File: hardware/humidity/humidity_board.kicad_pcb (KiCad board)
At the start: 2 copper layers, 99 x 20 mm, 23 parts, among them IC1 ATMEGA88-A, J1 RJ45, P1 ISP, P2 UART, SW1 SW_RESET, U1 ST485, U2 HYT271, m3_loch VAL**

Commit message: fill
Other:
- board size 99 x 20 mm -> 100 x 20 mm
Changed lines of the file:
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@@
     (area 7.399999 74 244.600001 124.2)
     (thickness 1.6)
-    (drawings 13)
+    (drawings 16)
     (tracks 271)
     (zones 0)
@@
     )
   )
+  (dimension 5 (width 0.3) (layer Cmts.User)
+    (gr_text "5.000 mm" (at 202.5 58.650001) (layer Cmts.User)
+      (effects (font (size 1.5 1.5) (thickness 0.3)))
+    )
+    (feature1 (pts (xy 200 88) (xy 200 57.300001)))
+    (feature2 (pts (xy 205 88) (xy 205 57.300001)))
+    (crossbar (pts (xy 205 60.000001) (xy 200 60.000001)))
+    (arrow1a (pts (xy 200 60.000001) (xy 201.126503 59.413581)))
+    (arrow1b (pts (xy 200 60.000001) (xy 201.126503 60.586421)))
+    (arrow2a (pts (xy 205 60.000001) (xy 203.873497 59.413581)))
+    (arrow2b (pts (xy 205 60.000001) (xy 203.873497 60.586421)))
+  )
+  (gr_line (start 200 106) (end 199 106) (angle 90) (layer Edge.Cuts) (width 0.1))
+  (gr_line (start 200 86) (end 200 106) (angle 90) (layer Edge.Cuts) (width 0.1))
+  (gr_line (start 199 86) (end 200 86) (angle 90) (layer Edge.Cuts) (width 0.1))
   (gr_line (start 199 106) (end 133.5 106) (angle 90) (layer Edge.Cuts) (width 0.1))
-  (gr_line (start 199 86) (end 199 106) (angle 90) (layer Edge.Cuts) (width 0.1))
   (gr_line (start 133.5 86) (end 199 86) (angle 90) (layer Edge.Cuts) (width 0.1))
   (dimension 100 (width 0.3) (layer Cmts.User)

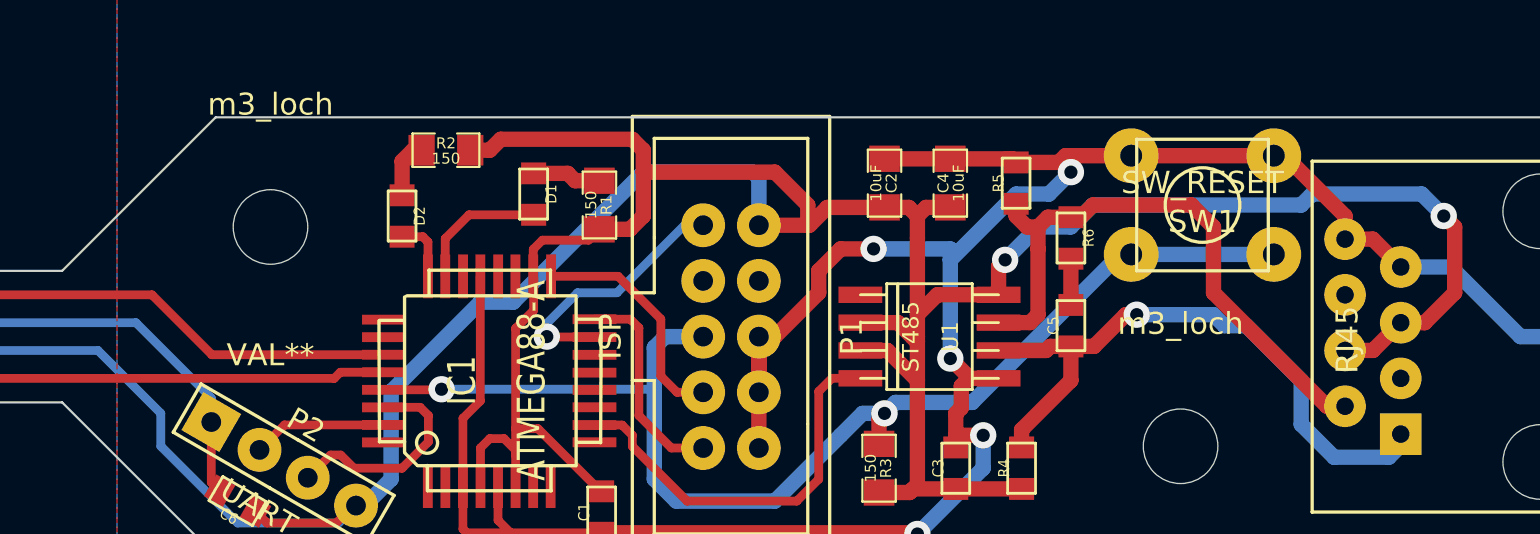
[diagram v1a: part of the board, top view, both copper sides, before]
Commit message: humidity led pos + zones
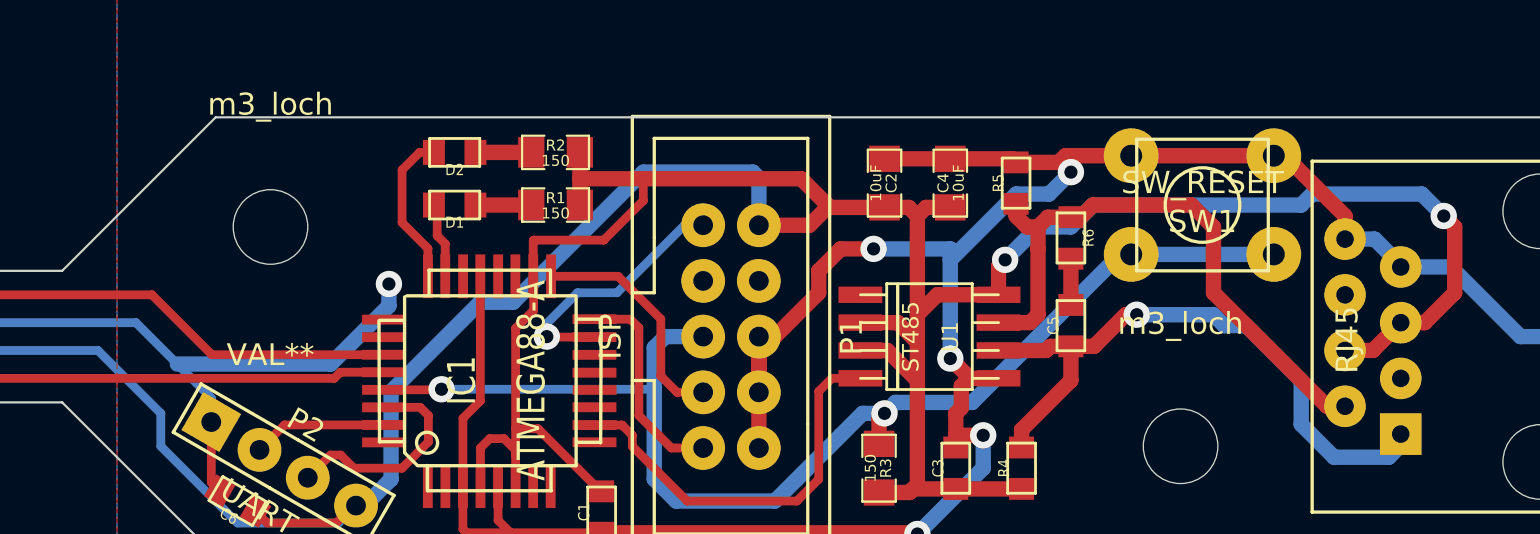
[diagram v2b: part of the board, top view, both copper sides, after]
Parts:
- moved R2 5.00 mm to (149.0, 87.6)
- moved D2 3.76 mm to (144.4, 87.6), turned to 180 degrees
- moved D1 3.63 mm to (144.4, 90.0), turned to 180 degrees
- moved R1 2.00 mm to (149.0, 90.0), turned to 0 degrees
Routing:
- net GND: track 170.8 -> 182.6 mm, vias 5 -> 6
- net VCC: track 196.3 -> 191.8 mm
- net /LED2: track 2.85 -> 7.13 mm
- net /LED1: track 6.20 -> 3.46 mm
- net N-0000016: track 3.14 -> 2.55 mm

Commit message: finalized boards for production
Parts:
- R3: value 150 -> 10k; footprint SM0805_big -> SM0603_big
- moved R3 0.05 mm to (163.7, 102.0)
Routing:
- net GND: track 182.6 -> 184.4 mm, vias 6 -> 5
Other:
- outline, holes or cut-outs redrawn

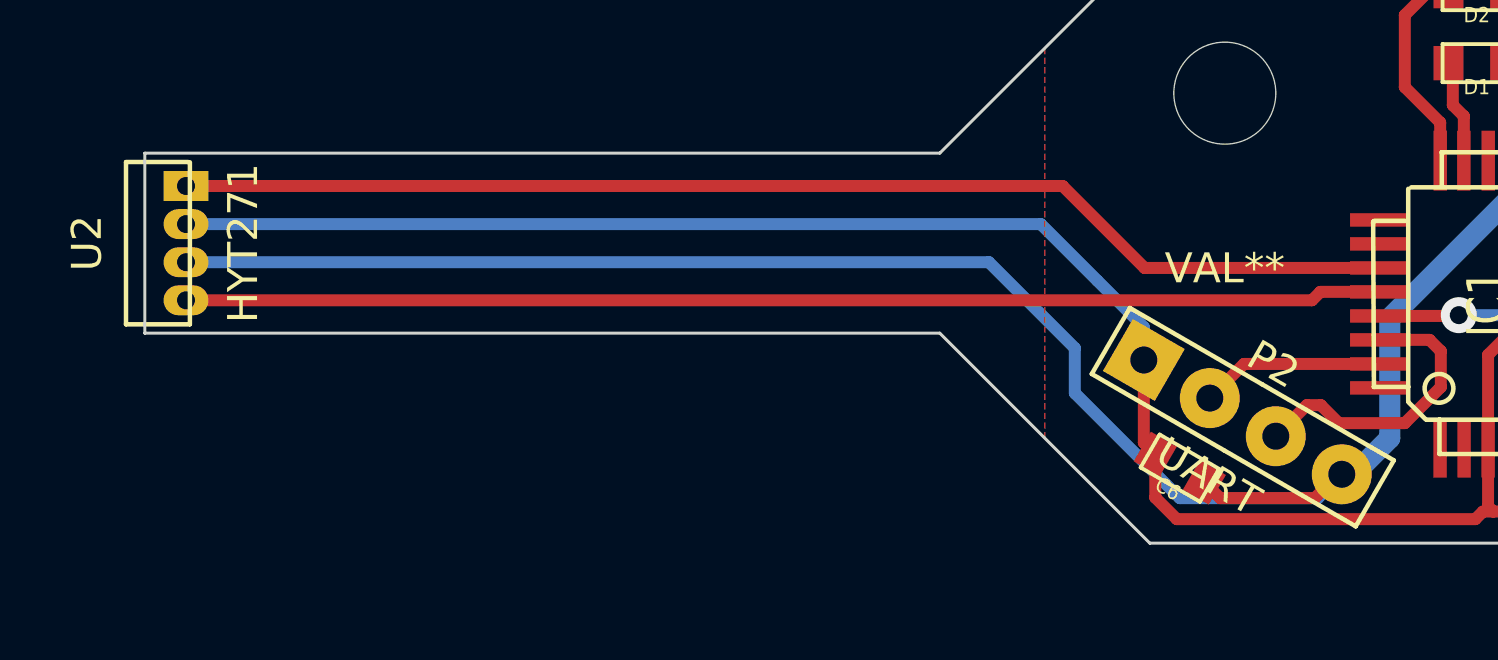
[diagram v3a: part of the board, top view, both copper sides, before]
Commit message: added i2c pullups to humidity board
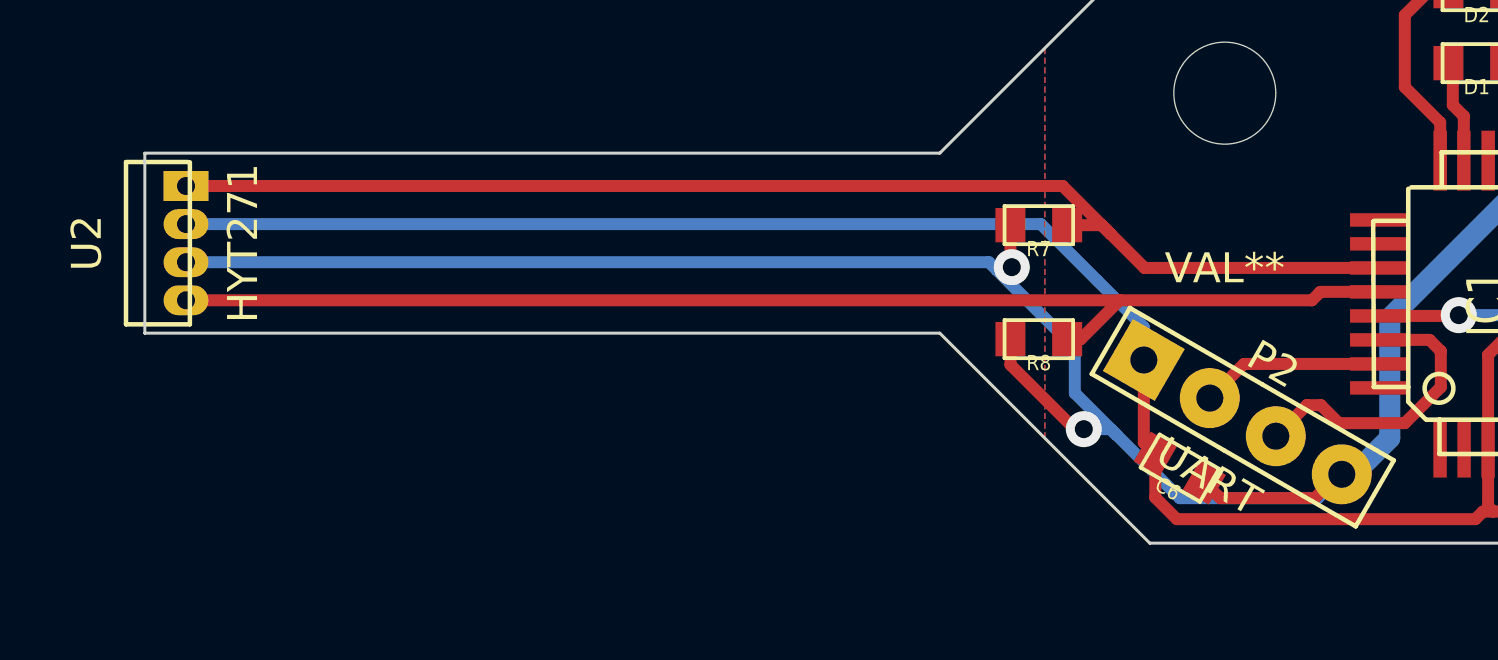
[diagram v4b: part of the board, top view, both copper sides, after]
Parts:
- added R7: 2k2, SM0603_big, F.Cu at (129.8, 95.4)
- added R8: 2k2, SM0603_big, F.Cu at (129.8, 99.2)
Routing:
- net VCC: track 191.8 -> 199.1 mm, vias 2 -> 4
- net /SCL: track 39.9 -> 42.2 mm
- net /SDA: track 40.9 -> 42.5 mm
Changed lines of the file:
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@@
 (kicad_pcb (version 3) (host pcbnew "(2013-may-18)-stable")
   (general
-    (links 62)
+    (links 66)
     (no_connects 0)
     (area 99.949999 85.949999 200.050001 106.050001)
     (thickness 1.6)
     (drawings 8)
-    (tracks 277)
+    (tracks 297)
     (zones 0)
-    (modules 23)
+    (modules 25)
     (nets 19)
   )
@@
   (net 13 /zb)
   (net 14 GND)
-  (net 15 N-0000014)
-  (net 16 N-0000015)
-  (net 17 N-0000016)
+  (net 15 N-0000015)
+  (net 16 N-0000017)
+  (net 17 N-000002)
   (net 18 VCC)
   (net_class Default "This is the default net class."
@@
     (add_net /zb)
     (add_net GND)
-    (add_net N-0000014)
     (add_net N-0000015)
-    (add_net N-0000016)
-    (add_net VCC)
+    (add_net N-0000017)
+    (add_net N-000002)
   )
   (net_class uc ""
@@
     (add_net /SDA)
     (add_net /TX)
+    (add_net VCC)
   )
   (module wannenstecker_2x5_rm254 (layer F.Cu)
@@
     (pad 1 smd rect (at -1.108 0) (size 1.2 1.397)
       (layers F.Cu F.Paste F.Mask)
-      (net 16 N-0000015)
+      (net 16 N-0000017)
     )
     (pad 2 smd rect (at 1.108 0) (size 1.2 1.397)
@@
     (pad 1 smd rect (at -1.108 0) (size 1.2 1.397)
       (layers F.Cu F.Paste F.Mask)
-      (net 17 N-0000016)
+      (net 17 N-000002)
     )
     (pad 2 smd rect (at 1.108 0) (size 1.2 1.397)
@@
     (pad 2 smd rect (at 0.945 0 90) (size 1 1.143)
       (layers F.Cu F.Paste F.Mask)
-      (net 15 N-0000014)
+      (net 15 N-0000015)
     )
     (model smd\resistors\R0603.wrl
@@
     (pad 1 smd rect (at -0.945 0 180) (size 1 1.143)
       (layers F.Cu F.Paste F.Mask)
-      (net 16 N-0000015)
+      (net 16 N-0000017)
     )
     (pad 2 smd rect (at 0.945 0 180) (size 1 1.143)
@@
     (pad 1 smd rect (at -0.945 0 180) (size 1 1.143)
       (layers F.Cu F.Paste F.Mask)
-      (net 17 N-0000016)
+      (net 17 N-000002)
     )
     (pad 2 smd rect (at 0.945 0 180) (size 1 1.143)
@@
     (pad 2 smd rect (at 0.945 0 270) (size 1 1.143)
       (layers F.Cu F.Paste F.Mask)
-      (net 15 N-0000014)
+      (net 15 N-0000015)
     )
     (model smd\resistors\R0603.wrl
@@
     )
     (pad 2 smd rect (at 0.945 0 270) (size 1 1.143)
+      (layers F.Cu F.Paste F.Mask)
+      (net 18 VCC)
+    )
+    (model smd\resistors\R0603.wrl
+      (at (xyz 0 0 0.001))
+      (scale (xyz 0.5 0.5 0.5))
+      (rotate (xyz 0 0 0))
+    )
+  )
+  (module SM0603_big (layer F.Cu)
+    (at 129.8 95.4 180)
+    (tags "SM0603 R")
+    (attr smd)
+    (fp_text reference R7 (at 0 -0.8 180) (layer F.SilkS)
+      (effects (font (size 0.508 0.4572) (thickness 0.1143)))
+    )
+    (fp_text value 2k2 (at 0 0 180) (layer F.SilkS) hide
+      (effects (font (size 0.508 0.4572) (thickness 0.1143)))
+    )
+    (fp_line (start -1.143 -0.635) (end 1.143 -0.635) (layer F.SilkS) (width 0.127))
+    (fp_line (start 1.143 -0.635) (end 1.143 0.635) (layer F.SilkS) (width 0.127))
+    (fp_line (start 1.143 0.635) (end -1.143 0.635) (layer F.SilkS) (width 0.127))
+    (fp_line (start -1.143 0.635) (end -1.143 -0.635) (layer F.SilkS) (width 0.127))
+    (pad 1 smd rect (at -0.945 0 180) (size 1 1.143)
+      (layers F.Cu F.Paste F.Mask)
+      (net 10 /SDA)
+    )
+    (pad 2 smd rect (at 0.945 0 180) (size 1 1.143)
+      (layers F.Cu F.Paste F.Mask)
+      (net 18 VCC)
+    )
+    (model smd\resistors\R0603.wrl
+      (at (xyz 0 0 0.001))
+      (scale (xyz 0.5 0.5 0.5))
+      (rotate (xyz 0 0 0))
+    )
+  )
+  (module SM0603_big (layer F.Cu)
+    (at 129.8 99.2 180)
+    (tags "SM0603 R")
+    (attr smd)
+    (fp_text reference R8 (at 0 -0.8 180) (layer F.SilkS)
+      (effects (font (size 0.508 0.4572) (thickness 0.1143)))
+    )
+    (fp_text value 2k2 (at 0 0 180) (layer F.SilkS) hide
+      (effects (font (size 0.508 0.4572) (thickness 0.1143)))
+    )
+    (fp_line (start -1.143 -0.635) (end 1.143 -0.635) (layer F.SilkS) (width 0.127))
+    (fp_line (start 1.143 -0.635) (end 1.143 0.635) (layer F.SilkS) (width 0.127))
+    (fp_line (start 1.143 0.635) (end -1.143 0.635) (layer F.SilkS) (width 0.127))
+    (fp_line (start -1.143 0.635) (end -1.143 -0.635) (layer F.SilkS) (width 0.127))
+    (pad 1 smd rect (at -0.945 0 180) (size 1 1.143)
+      (layers F.Cu F.Paste F.Mask)
+      (net 9 /SCL)
+    )
+    (pad 2 smd rect (at 0.945 0 180) (size 1 1.143)
       (layers F.Cu F.Paste F.Mask)
       (net 18 VCC)
@@
   (segment (start 153.8 95.2) (end 153.8 97.8) (width 0.4) (layer F.Cu) (net 8))
   (segment (start 151.8502 93.2502) (end 153.8 95.2) (width 0.4) (layer F.Cu) (net 8))
-  (segment (start 101.373 97.905) (end 138.905 97.905) (width 0.4) (layer F.Cu) (net 9) (status 10))
+  (segment (start 131.2 99.2) (end 130.745 99.2) (width 0.4) (layer F.Cu) (net 9))
+  (segment (start 132.495 97.905) (end 131.2 99.2) (width 0.4) (layer F.Cu) (net 9))
+  (segment (start 132.5 97.905) (end 132.495 97.905) (width 0.4) (layer F.Cu) (net 9))
+  (segment (start 132.5 97.905) (end 138.905 97.905) (width 0.4) (layer F.Cu) (net 9) (status 10))
+  (segment (start 101.373 97.905) (end 132.5 97.905) (width 0.4) (layer F.Cu) (net 9) (status 10))
   (segment (start 139.18592 97.62408) (end 141.174 97.62408) (width 0.4) (layer F.Cu) (net 9))
   (segment (start 138.905 97.905) (end 139.18592 97.62408) (width 0.4) (layer F.Cu) (net 9))
+  (segment (start 131.9 95.4) (end 132.2 95.7) (width 0.4) (layer F.Cu) (net 10))
+  (segment (start 130.745 95.4) (end 131.9 95.4) (width 0.4) (layer F.Cu) (net 10))
+  (segment (start 132.2 95.7) (end 133.32652 96.82652) (width 0.4) (layer F.Cu) (net 10))
   (segment (start 101.373 94.095) (end 130.595 94.095) (width 0.4) (layer F.Cu) (net 10))
   (segment (start 133.32652 96.82652) (end 141.174 96.82652) (width 0.4) (layer F.Cu) (net 10))
-  (segment (start 130.595 94.095) (end 133.32652 96.82652) (width 0.4) (layer F.Cu) (net 10))
+  (segment (start 130.595 94.095) (end 132.2 95.7) (width 0.4) (layer F.Cu) (net 10))
   (segment (start 141.174 100.02692) (end 136.638228 100.02692) (width 0.4) (layer F.Cu) (net 11))
   (segment (start 136.638228 100.02692) (end 135.500148 101.165) (width 0.4) (layer F.Cu) (net 11))
@@
   (segment (start 172.945 90.555) (end 173.5 90) (width 0.7) (layer F.Cu) (net 13))
   (segment (start 167.5 100.5) (end 168.1 100.5) (width 0.7) (layer F.Cu) (net 14))
-  (segment (start 163.155 104.945) (end 151.1 104.945) (width 0.7) (layer F.Cu) (net 14) (status 800000))
+  (segment (start 163.155 104.945) (end 151.1 104.945) (width 0.7) (layer F.Cu) (net 14))
   (segment (start 163.6 104.5) (end 163.155 104.945) (width 0.7) (layer F.Cu) (net 14))
   (segment (start 165.4 104.5) (end 163.6 104.5) (width 0.7) (layer F.Cu) (net 14))
@@
   (segment (start 145.345 87.6) (end 147.892 87.6) (width 0.7) (layer F.Cu) (net 16))
   (segment (start 145.345 90) (end 147.892 90) (width 0.7) (layer F.Cu) (net 17))
+  (segment (start 128.8 96.9) (end 128.4 96.9) (width 0.4) (layer B.Cu) (net 18))
+  (segment (start 128.9 96.8) (end 128.8 96.9) (width 0.4) (layer B.Cu) (net 18))
+  (via (at 128.9 96.8) (size 1.2) (layers F.Cu B.Cu) (net 18))
+  (segment (start 128.855 96.755) (end 128.9 96.8) (width 0.4) (layer F.Cu) (net 18))
+  (segment (start 128.855 95.4) (end 128.855 96.755) (width 0.4) (layer F.Cu) (net 18))
+  (segment (start 128.4 96.9) (end 131 99.5) (width 0.4) (layer B.Cu) (net 18))
+  (segment (start 132.2 102.2) (end 132.4 102.4) (width 0.4) (layer B.Cu) (net 18))
+  (segment (start 131.3 102.2) (end 132.2 102.2) (width 0.4) (layer B.Cu) (net 18))
+  (via (at 131.3 102.2) (size 1.2) (layers F.Cu B.Cu) (net 18))
+  (segment (start 131 102.2) (end 131.3 102.2) (width 0.4) (layer F.Cu) (net 18))
+  (segment (start 128.855 100.055) (end 131 102.2) (width 0.4) (layer F.Cu) (net 18))
+  (segment (start 128.855 99.2) (end 128.855 100.055) (width 0.4) (layer F.Cu) (net 18))
+  (segment (start 132.4 102.4) (end 134.5 104.5) (width 0.4) (layer B.Cu) (net 18))
   (segment (start 153 88.8) (end 160.2 88.8) (width 0.7) (layer F.Cu) (net 18))
   (segment (start 160.2 88.8) (end 161.508 90.108) (width 0.7) (layer F.Cu) (net 18))
@@
   (segment (start 139.104557 104.5) (end 139.899557 103.705) (width 0.4) (layer B.Cu) (net 18))
   (segment (start 134.5 104.5) (end 139.104557 104.5) (width 0.4) (layer B.Cu) (net 18))
-  (segment (start 131 101) (end 134.5 104.5) (width 0.4) (layer B.Cu) (net 18))
+  (segment (start 131 101) (end 132.4 102.4) (width 0.4) (layer B.Cu) (net 18))
   (segment (start 131 99.5) (end 131 101) (width 0.4) (layer B.Cu) (net 18))
-  (segment (start 128.135 96.635) (end 131 99.5) (width 0.4) (layer B.Cu) (net 18))
+  (segment (start 128.135 96.635) (end 128.4 96.9) (width 0.4) (layer B.Cu) (net 18))
   (segment (start 139.899557 103.705) (end 140.295 103.705) (width 0.7) (layer B.Cu) (net 18))
   (segment (start 158.27 88.77) (end 158.27 90.92) (width 0.7) (layer B.Cu) (net 18))

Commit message: for put all together
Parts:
- moved P2 89.4 mm to (204.6, 159.8)
- moved C1 89.4 mm to (219.1, 162.0)
- moved C2 89.4 mm to (232.0, 147.0)
- moved C3 89.4 mm to (235.2, 160.0)
- moved C4 89.4 mm to (235.0, 147.0)
- moved C5 89.4 mm to (240.5, 153.5)
- moved C6 89.4 mm to (202.5, 161.5)
- moved D1 89.4 mm to (212.4, 148.0)
- moved D2 89.4 mm to (212.4, 145.6)
- moved IC1 89.4 mm to (214.0, 156.0)
- moved J1 89.4 mm to (253.0, 154.0)
- moved P1 89.4 mm to (225.0, 154.0)
- moved R1 89.4 mm to (217.0, 148.0)
- moved R2 89.4 mm to (217.0, 145.6)
- moved R3 89.4 mm to (231.7, 160.0)
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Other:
- board text added: "V1.1"

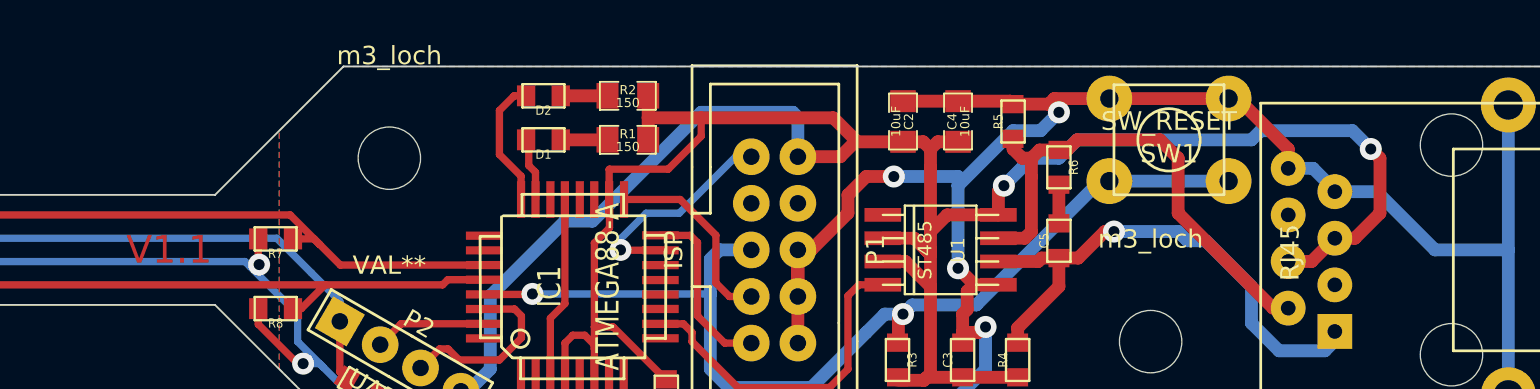
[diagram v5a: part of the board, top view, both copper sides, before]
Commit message: delete humility boards
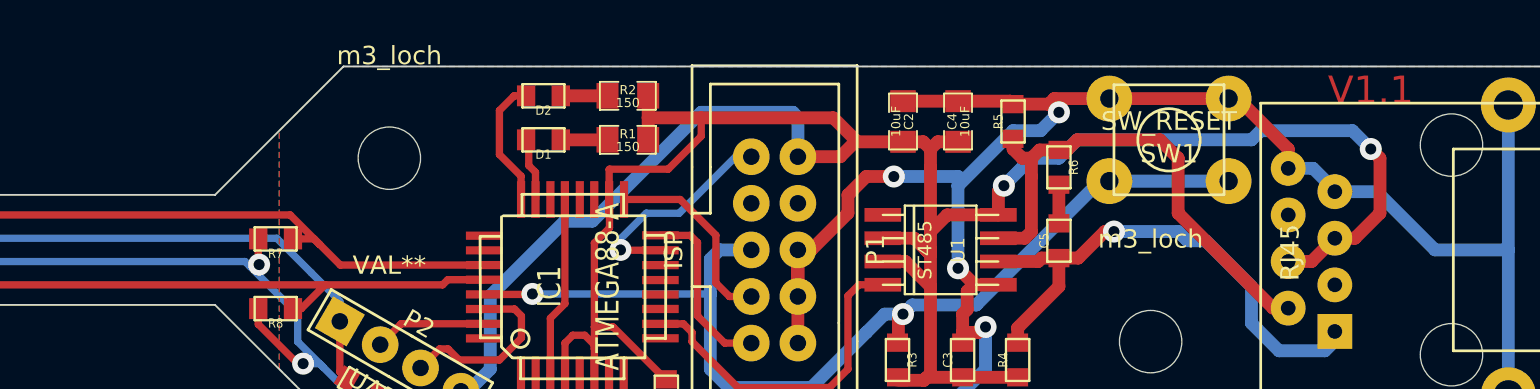
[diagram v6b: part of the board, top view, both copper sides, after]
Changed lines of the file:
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@@
     )
   )
-  (gr_text V1.1 (at 192 154) (layer F.Cu)
+  (gr_text V1.1 (at 257.5 145.3) (layer F.Cu)
     (effects (font (size 1.5 1.5) (thickness 0.3)))
   )

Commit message: 3 humidity boards but just 19 temperature
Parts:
- moved C1 343.9 mm to (498.1, 363.0)
- moved C2 343.9 mm to (511.0, 348.0)
- moved C3 343.9 mm to (514.2, 361.0)
- moved C4 343.9 mm to (514.0, 348.0)
- moved C5 343.9 mm to (519.5, 354.5)
- moved C6 343.9 mm to (481.5, 362.5)
- moved D1 343.9 mm to (491.4, 349.0)
- moved D2 343.9 mm to (491.4, 346.6)
- moved IC1 343.9 mm to (493.0, 357.0)
- moved J1 343.9 mm to (532.0, 355.0)
- moved P1 343.9 mm to (504.0, 355.0)
- moved P2 343.9 mm to (483.6, 360.8)
- moved R1 343.9 mm to (496.0, 349.0)
- moved R2 343.9 mm to (496.0, 346.6)
- moved R3 343.9 mm to (510.7, 361.0)
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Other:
- board text added: "v1.1"
- board text removed: "V1.1"
